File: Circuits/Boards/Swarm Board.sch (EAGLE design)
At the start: 65 parts, among them CON1 ISP(2X3), CON2 FTDI(1X6), T1 NPN2N2222, T2 NPN2N2222, T3 NPN2N2222, T4 TEFT4300, T5 TEFT4300, T6 TEFT4300, T7 TEFT4300, T8 TEFT4300, T9 TEFT4300, U1 ATMEGA324P, U2 MCP73832SOT-23, U3 TB6552FN/FNG

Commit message: updates to both boards and libraries. Added hall effect sensors to charger board
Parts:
- removed CON2: FTDI(1X6), Mechanical:FTDI(1X6)
- removed LED10: (no value), Passive:LED0603
- removed R27: (no value), Passive:RES0603
- added U$1: MAIN_CONNECTOR, Mechanical:MAIN_CONNECTOR
- added U$2: FTDI_3PIN, Mechanical:FTDI_3PIN
- R3: value 400 -> 2k
- R4: value 600 -> 3k
- R5: value 10k -> 7k
- R6: value 15k -> 18k
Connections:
- removed net LED3: R27.1
- removed net N$22: LED10.C, R27.2
- removed net N$23: C9.2
- removed net N$24: LED10.A, LED8.A
- net +3V: now also LED8.A
- net +VBAT: now also U$1.BAT+
- net GND: now also C9.2, U$1.BAT-, U$2.GND; no longer CON2.GND
- net MA+: now also U$1.MA+
- net MA-: now also U$1.MA-
- net MB+: now also U$1.MB+
- net MB-: now also U$1.MB-
- net N$7: now also U$2.RXI; no longer CON2.RXI
- net N$8: now also U$2.TXO; no longer CON2.TXO
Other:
- moved on the sheet: C4, C5, C6, C7, LED1, LED13, LED2, LED3, LED4, LED5, LED6, LED7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

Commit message: 
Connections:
- net N$7 renamed DATAANTENNA
- net +3V: now also R2.2
- net +VCHG: no longer R2.2
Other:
- note added: "Antenna connections"
- moved on the sheet: LED1, R2
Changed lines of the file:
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@@
 <part name="U$1" library="Mechanical" deviceset="MAIN_CONNECTOR" device=""/>
 <part name="U$2" library="Mechanical" deviceset="FTDI_3PIN" device=""/>
+<part name="P+15" library="Supply" deviceset="+VCHG" device=""/>
+<part name="GND18" library="Supply" deviceset="GND" device=""/>
+<part name="P+16" library="Supply" deviceset="+3V" device=""/>
 </parts>
 <sheets>
@@
 <plain>
 <text x="-127" y="127" size="1.778" layer="97">4.6v ideal</text>
+<text x="-281.94" y="-33.02" size="1.778" layer="97">Antenna connections</text>
 </plain>
 <instances>
@@
 <instance part="C4" gate="G$1" x="-71.12" y="93.98"/>
 <instance part="C5" gate="G$1" x="-109.22" y="86.36"/>
-<instance part="R2" gate="G$1" x="-116.84" y="109.22" rot="R90"/>
+<instance part="R2" gate="G$1" x="-137.16" y="111.76" rot="R90"/>
 <instance part="R3" gate="G$1" x="-127" y="109.22" rot="R90"/>
 <instance part="R4" gate="G$1" x="-127" y="93.98" rot="R90"/>
@@
 <instance part="C7" gate="G$1" x="309.88" y="154.94"/>
 <instance part="P+10" gate="1" x="309.88" y="190.5"/>
-<instance part="LED1" gate="G$1" x="-116.84" y="99.06"/>
+<instance part="LED1" gate="G$1" x="-137.16" y="101.6"/>
 <instance part="T4" gate="G$1" x="373.38" y="210.82"/>
 <instance part="T5" gate="G$1" x="393.7" y="210.82"/>
@@
 <instance part="U$1" gate="G$1" x="114.3" y="-106.68"/>
 <instance part="U$2" gate="G$1" x="93.98" y="-15.24"/>
+<instance part="P+15" gate="G$1" x="-251.46" y="-48.26" rot="R270"/>
+<instance part="GND18" gate="1" x="-248.92" y="-63.5" rot="R90"/>
+<instance part="P+16" gate="1" x="-137.16" y="121.92"/>
 </instances>
 <busses>
@@
 <junction x="-160.02" y="-17.78"/>
 </segment>
+<segment>
+<pinref part="R2" gate="G$1" pin="2"/>
+<wire x1="-137.16" y1="116.84" x2="-137.16" y2="119.38" width="0.1524" layer="91"/>
+<pinref part="P+16" gate="1" pin="+3V"/>
+</segment>
 </net>
 <net name="GND" class="0">
@@
 <label x="88.9" y="-106.68" size="1.778" layer="91" rot="R180" xref="yes"/>
 </segment>
+<segment>
+<pinref part="GND18" gate="1" pin="GND"/>
+<wire x1="-251.46" y1="-63.5" x2="-271.78" y2="-63.5" width="0.1524" layer="91"/>
+</segment>
 </net>
 <net name="+VBAT" class="0">
@@
 </segment>
 </net>
-<net name="CHGSTATUS" class="0">
-<segment>
-<pinref part="U2" gate="G$1" pin="STAT"/>
-<wire x1="-104.14" y1="93.98" x2="-116.84" y2="93.98" width="0.1524" layer="91"/>
-<label x="-147.32" y="93.98" size="1.778" layer="91" rot="R180" xref="yes"/>
-<pinref part="LED1" gate="G$1" pin="C"/>
-<wire x1="-116.84" y1="93.98" x2="-147.32" y2="93.98" width="0.1524" layer="91"/>
-<junction x="-116.84" y="93.98"/>
-</segment>
-</net>
 <net name="+VCHG" class="0">
 <segment>
-<pinref part="P+4" gate="G$1" pin="+VCHG"/>
-<pinref part="R2" gate="G$1" pin="2"/>
-<wire x1="-116.84" y1="116.84" x2="-116.84" y2="114.3" width="0.1524" layer="91"/>
+<pinref part="P+15" gate="G$1" pin="+VCHG"/>
+<wire x1="-251.46" y1="-48.26" x2="-271.78" y2="-48.26" width="0.1524" layer="91"/>
+</segment>
+<segment>
 <pinref part="C5" gate="G$1" pin="1"/>
 <wire x1="-109.22" y1="91.44" x2="-109.22" y2="99.06" width="0.1524" layer="91"/>
 <wire x1="-109.22" y1="99.06" x2="-109.22" y2="114.3" width="0.1524" layer="91"/>
-<wire x1="-109.22" y1="114.3" x2="-116.84" y2="114.3" width="0.1524" layer="91"/>
 <pinref part="U2" gate="G$1" pin="VDD"/>
 <wire x1="-104.14" y1="99.06" x2="-109.22" y2="99.06" width="0.1524" layer="91"/>
@@
 <pinref part="R3" gate="G$1" pin="2"/>
 <wire x1="-127" y1="114.3" x2="-116.84" y2="114.3" width="0.1524" layer="91"/>
+<pinref part="P+4" gate="G$1" pin="+VCHG"/>
+<wire x1="-116.84" y1="114.3" x2="-109.22" y2="114.3" width="0.1524" layer="91"/>
+<wire x1="-116.84" y1="116.84" x2="-116.84" y2="114.3" width="0.1524" layer="91"/>
 <junction x="-116.84" y="114.3"/>
 </segment>
@@
 <segment>
 <pinref part="R2" gate="G$1" pin="1"/>
-<wire x1="-116.84" y1="104.14" x2="-116.84" y2="101.6" width="0.1524" layer="91"/>
+<wire x1="-137.16" y1="106.68" x2="-137.16" y2="104.14" width="0.1524" layer="91"/>
 <pinref part="LED1" gate="G$1" pin="A"/>
 </segment>
@@
 </segment>
 </net>
-<net name="N$7" class="0">
-<segment>
-<wire x1="83.82" y1="-12.7" x2="55.88" y2="-12.7" width="0.1524" layer="91"/>
+<net name="DATAANTENNA" class="0">
+<segment>
+<wire x1="83.82" y1="-12.7" x2="76.2" y2="-12.7" width="0.1524" layer="91"/>
+<wire x1="76.2" y1="-12.7" x2="55.88" y2="-12.7" width="0.1524" layer="91"/>
 <wire x1="55.88" y1="-12.7" x2="43.18" y2="-25.4" width="0.1524" layer="91"/>
 <pinref part="U1" gate="G$1" pin="PD1(PCINT25/TXD0)"/>
 <wire x1="43.18" y1="-25.4" x2="30.48" y2="-25.4" width="0.1524" layer="91"/>
 <pinref part="U$2" gate="G$1" pin="RXI"/>
+<wire x1="76.2" y1="-12.7" x2="76.2" y2="-2.54" width="0.1524" layer="91"/>
+<wire x1="76.2" y1="-2.54" x2="88.9" y2="-2.54" width="0.1524" layer="91"/>
+<label x="88.9" y="-2.54" size="1.778" layer="91" xref="yes"/>
+<junction x="76.2" y="-12.7"/>
+</segment>
+<segment>
+<wire x1="-251.46" y1="-55.88" x2="-271.78" y2="-55.88" width="0.1524" layer="91"/>
+<label x="-251.46" y="-55.88" size="1.778" layer="91" xref="yes"/>
 </segment>
 </net>
@@
 </segment>
 </net>
+<net name="CHGSTATUS" class="0">
+<segment>
+<pinref part="U2" gate="G$1" pin="STAT"/>
+<wire x1="-104.14" y1="93.98" x2="-137.16" y2="93.98" width="0.1524" layer="91"/>
+<pinref part="LED1" gate="G$1" pin="C"/>
+<wire x1="-137.16" y1="93.98" x2="-137.16" y2="96.52" width="0.1524" layer="91"/>
+<wire x1="-137.16" y1="93.98" x2="-147.32" y2="93.98" width="0.1524" layer="91"/>
+<label x="-147.32" y="93.98" size="1.778" layer="91" rot="R180" xref="yes"/>
+</segment>
+</net>

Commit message: 
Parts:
- added R27: (no value), Passive:RES0603
- added T10: TEFT4300, Passive:TEFT4300
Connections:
- net R_A renamed FL
- removed net R_D: R18.2, R19.2, R20.2, R21.2, R24.2, T5.E, T6.E, T7.E, T8.E, T9.E
- new net BL: R20.2, T7.E
- new net BM: R21.2, T8.E
- new net BR: R24.2, T9.E
- new net DISTANCERECEIVE: R27.2, T10.E, U1.PA4(ADC4/PCINT4)
- new net FM: R18.2, T5.E
- new net FR: R19.2, T6.E
- net +3V: now also T10.C
- net GND: now also R27.1
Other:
- moved on the sheet: C6, C7, LED13, LED2, LED3, LED4, LED5, LED6, LED7, R10, R11, R12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

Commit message: updates to both boards
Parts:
- added R29, R31: 10k, Passive:RES0603
- added R30, R32: 1k, Passive:RES0603
- added R33, R34, R35: (no value), Passive:RES0603
- added T11, T12: NPN2N2222, Passive:NPN2N2222
- R2: value 1.5k -> 750
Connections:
- removed net AIN1: U3.AIN1
- removed net BIN1: U3.BIN1
- new net AIN: R30.1, U3.AIN1
- new net AIN3: R31.2, T12.C
- new net BIN: R32.1, U3.BIN1
- new net BUMPER: R35.2, U$1.BUMP, U1.PA4(ADC4/PCINT4)
- new net IRENABLE: U$1.ENABLE
- new net N$22: R30.2, T11.B
- new net N$7: R32.2, T12.B
- net +3V: now also R29.1, R31.1, U$1.+3V
- net AIN2: now also R29.2, T11.C
- net DISTANCERECEIVE: now also U1.PA5(ADC5/PCINT5); no longer U1.PA4(ADC4/PCINT4)
- net GND: now also R33.1, R34.1, R35.1, T11.E, T12.E, U$1.GND
- net LINESENSE1: now also R33.2, U$1.LINER
- net LINESENSE2: now also R34.2, U$1.LINEL

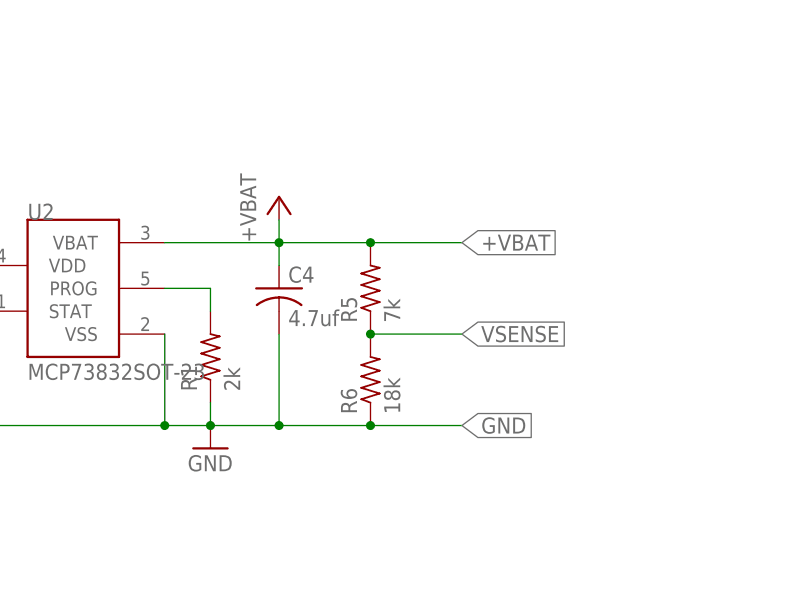
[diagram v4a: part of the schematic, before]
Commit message: 
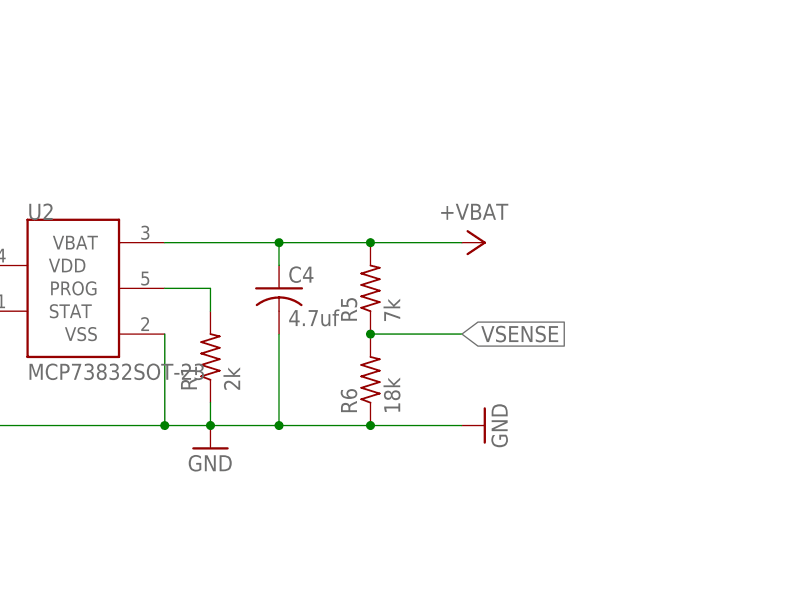
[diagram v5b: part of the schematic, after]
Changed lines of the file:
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@@
 <part name="P+1" library="Supply" deviceset="+3V" device=""/>
 <part name="P+2" library="Supply" deviceset="+VBAT" device=""/>
-<part name="P+3" library="Supply" deviceset="+VBAT" device=""/>
 <part name="P+4" library="Supply" deviceset="+VCHG" device=""/>
 <part name="GND1" library="Supply" deviceset="GND" device=""/>
@@
 <part name="GND24" library="Supply" deviceset="GND" device=""/>
 <part name="GND25" library="Supply" deviceset="GND" device=""/>
+<part name="GND26" library="Supply" deviceset="GND" device=""/>
+<part name="P+21" library="Supply" deviceset="+VBAT" device=""/>
 </parts>
 <sheets>
@@
 <instance part="P+1" gate="1" x="50.8" y="106.68"/>
 <instance part="P+2" gate="G$1" x="10.16" y="104.14"/>
-<instance part="P+3" gate="G$1" x="-71.12" y="104.14"/>
 <instance part="P+4" gate="G$1" x="-116.84" y="116.84"/>
 <instance part="GND1" gate="1" x="-55.88" y="25.4"/>
@@
 <instance part="GND24" gate="1" x="93.98" y="-139.7"/>
 <instance part="GND25" gate="1" x="99.06" y="-139.7"/>
+<instance part="GND26" gate="1" x="-48.26" y="81.28" rot="R90"/>
+<instance part="P+21" gate="G$1" x="-50.8" y="101.6" rot="R270"/>
 </instances>
 <busses>
@@
 <wire x1="-71.12" y1="81.28" x2="-71.12" y2="91.44" width="0.1524" layer="91"/>
 <wire x1="-71.12" y1="81.28" x2="-60.96" y2="81.28" width="0.1524" layer="91"/>
-<label x="-50.8" y="81.28" size="1.778" layer="91" xref="yes"/>
 <wire x1="-60.96" y1="81.28" x2="-50.8" y2="81.28" width="0.1524" layer="91"/>
 <wire x1="-71.12" y1="81.28" x2="-78.74" y2="81.28" width="0.1524" layer="91"/>
@@
 <pinref part="R6" gate="G$1" pin="1"/>
 <junction x="-60.96" y="81.28"/>
+<pinref part="GND26" gate="1" pin="GND"/>
 </segment>
 <segment>
@@
 <wire x1="-83.82" y1="101.6" x2="-71.12" y2="101.6" width="0.1524" layer="91"/>
 <wire x1="-71.12" y1="101.6" x2="-71.12" y2="99.06" width="0.1524" layer="91"/>
-<wire x1="-71.12" y1="101.6" x2="-71.12" y2="104.14" width="0.1524" layer="91"/>
-<pinref part="P+3" gate="G$1" pin="+VBAT"/>
 <junction x="-71.12" y="101.6"/>
 <wire x1="-71.12" y1="101.6" x2="-60.96" y2="101.6" width="0.1524" layer="91"/>
-<label x="-50.8" y="101.6" size="1.778" layer="91" xref="yes"/>
 <pinref part="R5" gate="G$1" pin="2"/>
 <wire x1="-60.96" y1="101.6" x2="-50.8" y2="101.6" width="0.1524" layer="91"/>
 <junction x="-60.96" y="101.6"/>
-</segment>
-<segment>
+<pinref part="P+21" gate="G$1" pin="+VBAT"/>
+</segment>
+<segment>

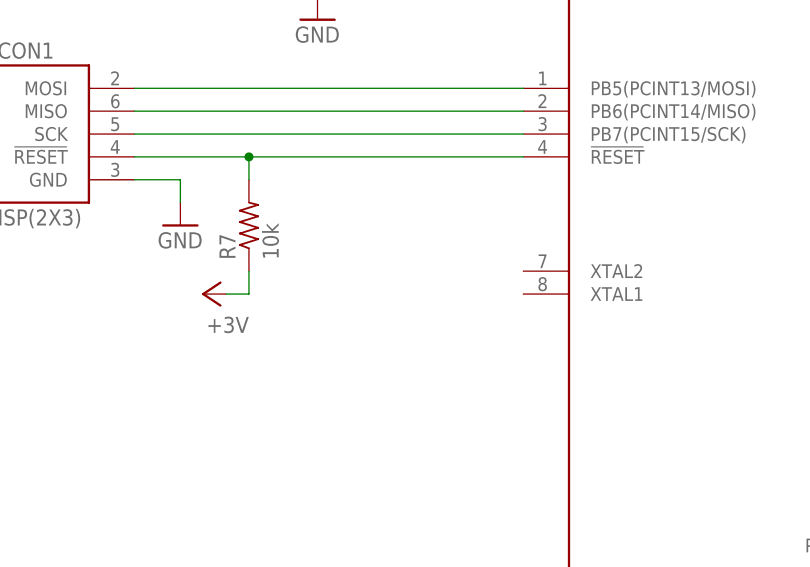
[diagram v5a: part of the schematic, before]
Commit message: 
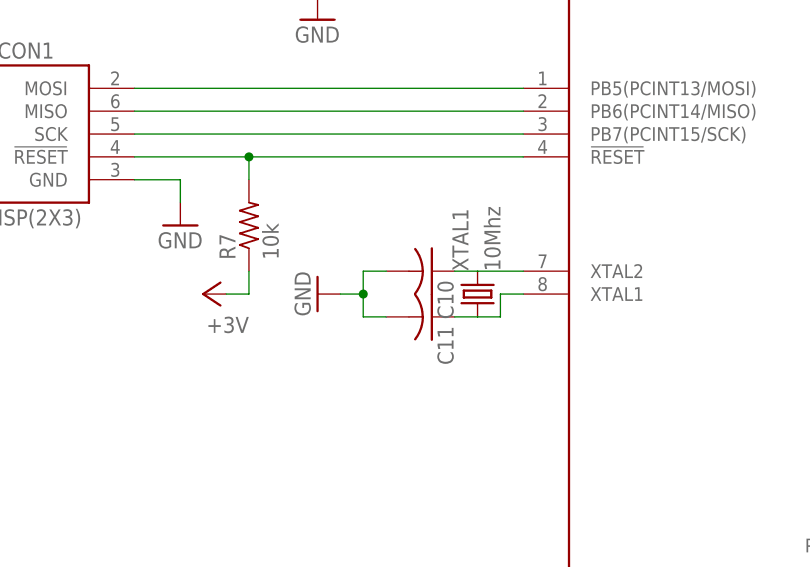
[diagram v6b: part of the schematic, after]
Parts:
- added C10, C11: (no value), Passive:CAP0603
- added XTAL1: 10Mhz, Passive:NX5032GA-10.000000MHZ
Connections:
- new net N$23: C10.1, U1.XTAL2, XTAL1.2
- new net N$24: C11.1, U1.XTAL1, XTAL1.1
- net GND: now also C10.2, C11.2
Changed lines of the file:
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@@
 <part name="GND26" library="Supply" deviceset="GND" device=""/>
 <part name="P+21" library="Supply" deviceset="+VBAT" device=""/>
+<part name="XTAL1" library="Passive" deviceset="NX5032GA-10.000000MHZ" device="" value="10Mhz"/>
+<part name="C10" library="Passive" deviceset="CAP" device="0603"/>
+<part name="C11" library="Passive" deviceset="CAP" device="0603"/>
+<part name="GND27" library="Supply" deviceset="GND" device=""/>
 </parts>
 <sheets>
@@
 <instance part="GND26" gate="1" x="-48.26" y="81.28" rot="R90"/>
 <instance part="P+21" gate="G$1" x="-50.8" y="101.6" rot="R270"/>
+<instance part="XTAL1" gate="G$1" x="-38.1" y="-5.08" rot="R90"/>
+<instance part="C10" gate="G$1" x="-45.72" y="-2.54" rot="R270"/>
+<instance part="C11" gate="G$1" x="-45.72" y="-7.62" rot="R270"/>
+<instance part="GND27" gate="1" x="-55.88" y="-5.08" rot="R270"/>
 </instances>
 <busses>
@@
 <pinref part="GND25" gate="1" pin="GND"/>
 </segment>
+<segment>
+<pinref part="C10" gate="G$1" pin="2"/>
+<wire x1="-48.26" y1="-2.54" x2="-50.8" y2="-2.54" width="0.1524" layer="91"/>
+<wire x1="-50.8" y1="-2.54" x2="-50.8" y2="-5.08" width="0.1524" layer="91"/>
+<pinref part="C11" gate="G$1" pin="2"/>
+<wire x1="-50.8" y1="-5.08" x2="-50.8" y2="-7.62" width="0.1524" layer="91"/>
+<wire x1="-48.26" y1="-7.62" x2="-50.8" y2="-7.62" width="0.1524" layer="91"/>
+<wire x1="-50.8" y1="-5.08" x2="-53.34" y2="-5.08" width="0.1524" layer="91"/>
+<pinref part="GND27" gate="1" pin="GND"/>
+<junction x="-50.8" y="-5.08"/>
+</segment>
 </net>
 <net name="+VBAT" class="0">
@@
 </segment>
 </net>
+<net name="N$23" class="0">
+<segment>
+<pinref part="U1" gate="G$1" pin="XTAL2"/>
+<pinref part="XTAL1" gate="G$1" pin="2"/>
+<wire x1="-33.02" y1="-2.54" x2="-38.1" y2="-2.54" width="0.1524" layer="91"/>
+<wire x1="-38.1" y1="-2.54" x2="-40.64" y2="-2.54" width="0.1524" layer="91"/>
+<pinref part="C10" gate="G$1" pin="1"/>
+</segment>
+</net>
+<net name="N$24" class="0">
+<segment>
+<pinref part="U1" gate="G$1" pin="XTAL1"/>
+<wire x1="-33.02" y1="-5.08" x2="-35.56" y2="-5.08" width="0.1524" layer="91"/>
+<pinref part="XTAL1" gate="G$1" pin="1"/>
+<wire x1="-35.56" y1="-5.08" x2="-35.56" y2="-7.62" width="0.1524" layer="91"/>
+<wire x1="-35.56" y1="-7.62" x2="-38.1" y2="-7.62" width="0.1524" layer="91"/>
+<wire x1="-38.1" y1="-7.62" x2="-40.64" y2="-7.62" width="0.1524" layer="91"/>
+<pinref part="C11" gate="G$1" pin="1"/>
+</segment>
+</net>

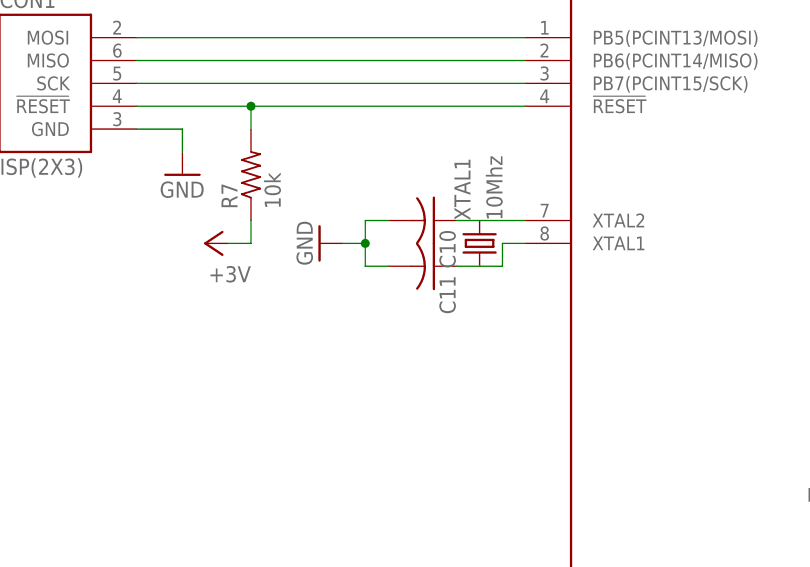
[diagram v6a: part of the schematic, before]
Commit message: 
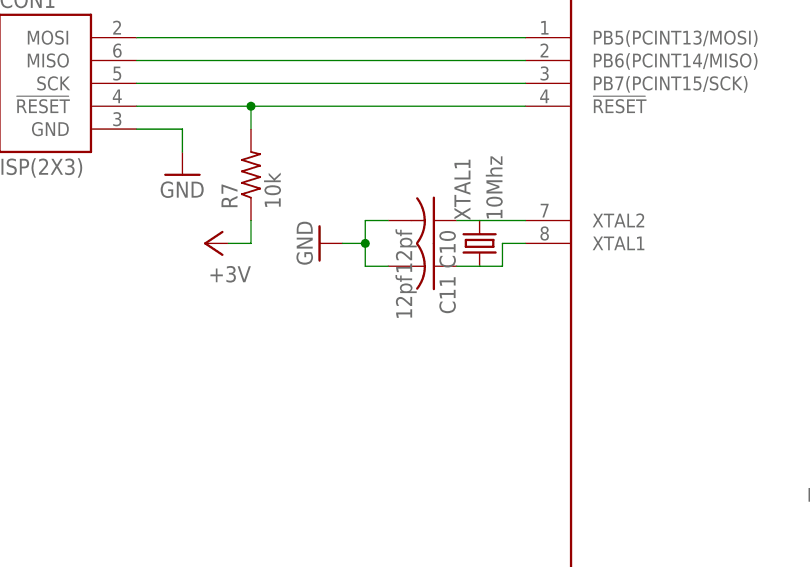
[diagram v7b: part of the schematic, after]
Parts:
- C10, C11: value (none) -> 12pf
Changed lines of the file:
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@@
 <part name="P+21" library="Supply" deviceset="+VBAT" device=""/>
 <part name="XTAL1" library="Passive" deviceset="NX5032GA-10.000000MHZ" device="" value="10Mhz"/>
-<part name="C10" library="Passive" deviceset="CAP" device="0603"/>
-<part name="C11" library="Passive" deviceset="CAP" device="0603"/>
+<part name="C10" library="Passive" deviceset="CAP" device="0603" value="12pf"/>
+<part name="C11" library="Passive" deviceset="CAP" device="0603" value="12pf"/>
 <part name="GND27" library="Supply" deviceset="GND" device=""/>
 </parts>

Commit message: 
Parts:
- LED1, LED8: value (none) -> red
- LED9: value (none) -> green
- R16, R23: value 500 -> 1k
- R25, R26: value (none) -> 750
- R28: value (none) -> 1k
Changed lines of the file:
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@@
 <part name="R14" library="Passive" deviceset="RES" device="0603"/>
 <part name="R15" library="Passive" deviceset="RES" device="0603"/>
-<part name="R16" library="Passive" deviceset="RES" device="0603" value="500"/>
+<part name="R16" library="Passive" deviceset="RES" device="0603" value="1k"/>
 <part name="GND8" library="Supply" deviceset="GND" device=""/>
 <part name="LED2" library="Passive" deviceset="LED" device="5MMRA" value="IR"/>
@@
 <part name="T3" library="Passive" deviceset="NPN2N2222" device=""/>
 <part name="R22" library="Passive" deviceset="RES" device="0603"/>
-<part name="R23" library="Passive" deviceset="RES" device="0603" value="500"/>
+<part name="R23" library="Passive" deviceset="RES" device="0603" value="1k"/>
 <part name="GND9" library="Supply" deviceset="GND" device=""/>
 <part name="LED13" library="Passive" deviceset="LED" device="5MMRA" value="IR"/>
 <part name="C7" library="Passive" deviceset="CAP" device="0805" value="10uf"/>
 <part name="P+10" library="Supply" deviceset="+3V" device=""/>
-<part name="LED1" library="Passive" deviceset="LED" device="0603"/>
+<part name="LED1" library="Passive" deviceset="LED" device="0603" value="red"/>
 <part name="T4" library="Passive" deviceset="TEFT4300" device=""/>
 <part name="T5" library="Passive" deviceset="TEFT4300" device=""/>
@@
 <part name="P+12" library="Supply" deviceset="+3V" device=""/>
 <part name="P+13" library="Supply" deviceset="+VBAT" device=""/>
-<part name="LED8" library="Passive" deviceset="LED" device="0603"/>
-<part name="R25" library="Passive" deviceset="RES" device="0603"/>
-<part name="LED9" library="Passive" deviceset="LED" device="0603"/>
-<part name="R26" library="Passive" deviceset="RES" device="0603"/>
+<part name="LED8" library="Passive" deviceset="LED" device="0603" value="red"/>
+<part name="R25" library="Passive" deviceset="RES" device="0603" value="750"/>
+<part name="LED9" library="Passive" deviceset="LED" device="0603" value="green"/>
+<part name="R26" library="Passive" deviceset="RES" device="0603" value="750"/>
 <part name="P+14" library="Supply" deviceset="+3V" device=""/>
-<part name="R28" library="Passive" deviceset="RES" device="0603"/>
+<part name="R28" library="Passive" deviceset="RES" device="0603" value="1k"/>
 <part name="U$1" library="Mechanical" deviceset="MAIN_CONNECTOR" device=""/>
 <part name="U$2" library="Mechanical" deviceset="FTDI_3PIN" device=""/>
